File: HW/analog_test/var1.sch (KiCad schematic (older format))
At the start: 30 parts, among them P1 Line Out, P2 POWER, Q1 2N5551, Q2 2N5551, Q3 2N5551, SW1 PBH2UEESNPNAGV1RBLK

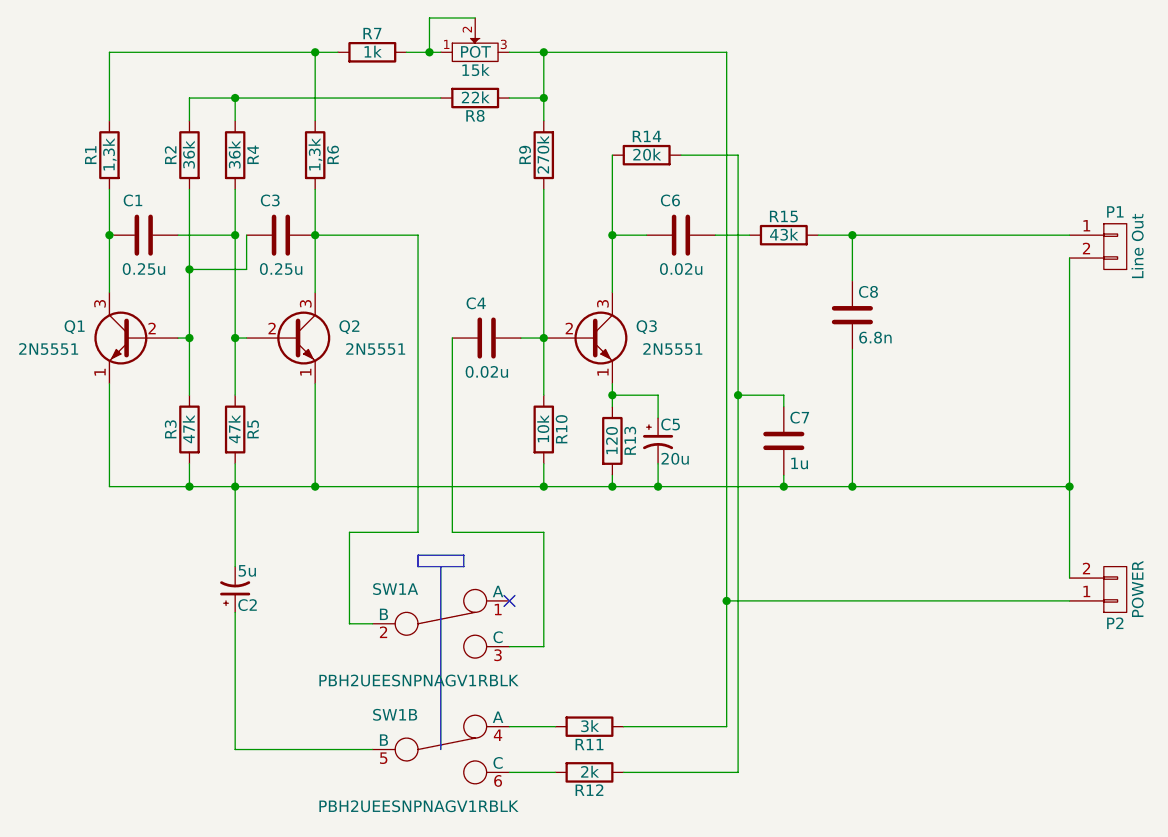
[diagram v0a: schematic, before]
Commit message: HW: Analog synth1: fixed error in schematics after some real testing
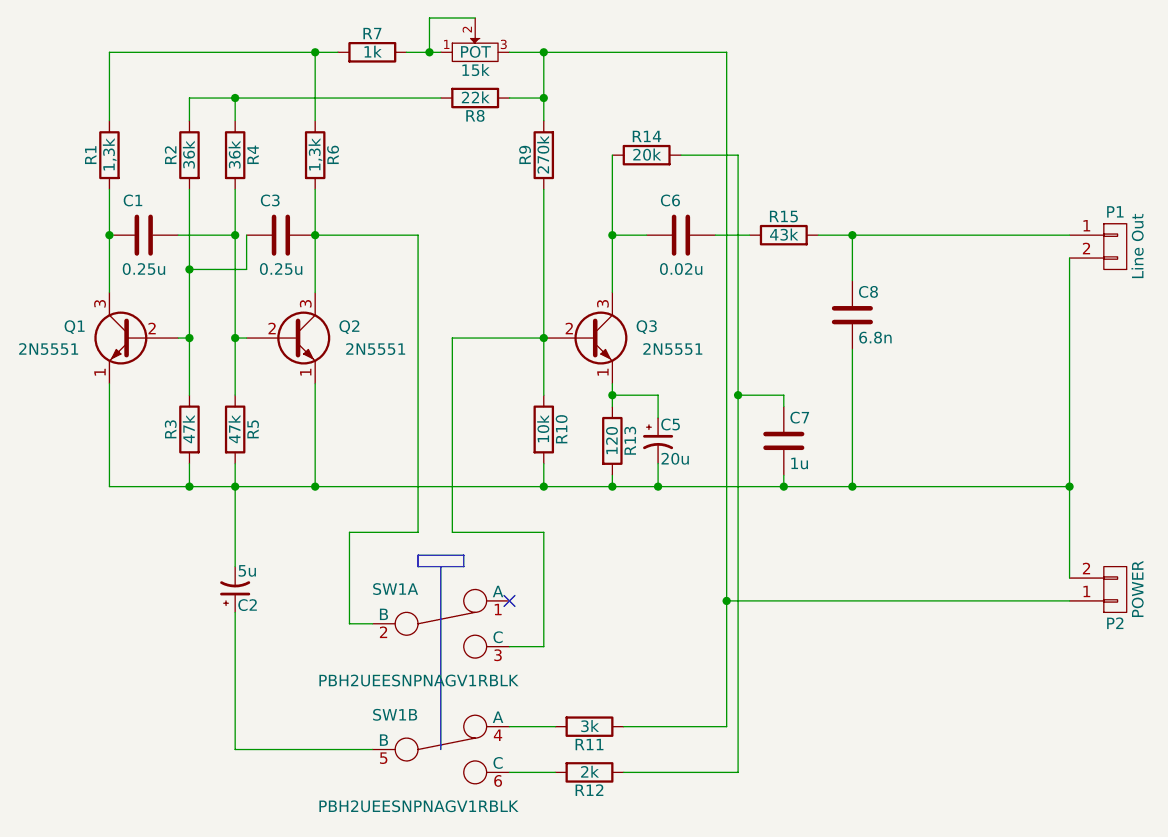
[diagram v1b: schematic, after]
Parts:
- removed C4: 0.02u, symbol C
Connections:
- net at Q3.2 (B), R10.1, R9.1: now also SW1.3 (C)
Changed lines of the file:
@@
 LIBS:contrib
 LIBS:valves
+LIBS:analog_test-cache
 EELAYER 25 0
 EELAYER END
@@
 $EndComp
 $Comp
-L C C4
-U 1 1 5C98983F
-P 4450 2400
-F 0 "C4" V 4600 2400 50  0000 L CNN
-F 1 "0.02u" V 4300 2300 50  0000 L CNN
-F 2 "" H 4488 2250 50  0000 C CNN
-F 3 "" H 4450 2400 50  0000 C CNN
-	1    4450 2400
-	0    -1   -1   0
-$EndComp
-$Comp
 L R R13
 U 1 1 5C989C21
@@
 Connection ~ 3700 3050
 Wire Wire Line
-	4600 2400 4700 2400
+	4300 2400 4700 2400
 Wire Wire Line
 	3700 1950 4150 1950
